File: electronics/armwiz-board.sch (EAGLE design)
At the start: 86 parts, among them J1 MICRO-SDCARD-CONNECTOR-330006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, U1 STM32F10XRXT6, U4 MIC5219-3.3V, X1 FH12-12S-1S, Y1 16MHz

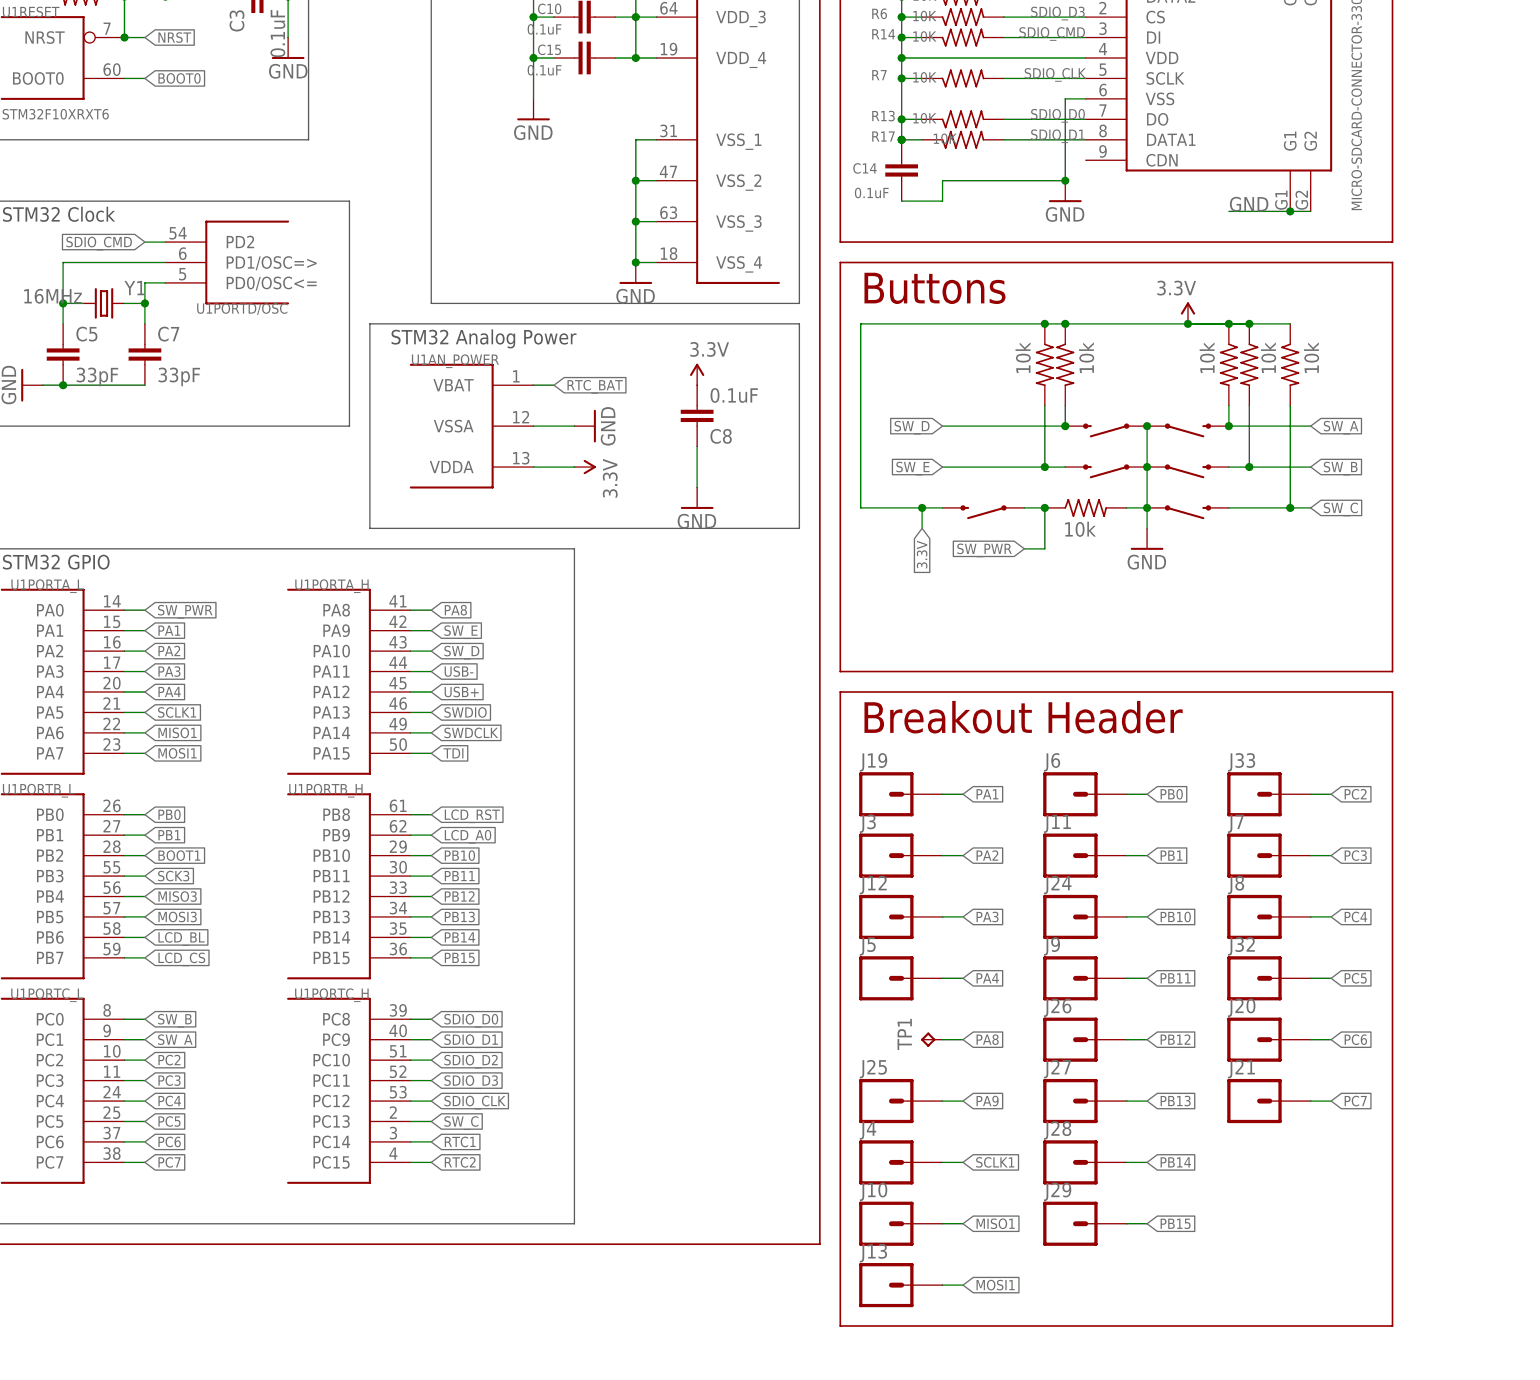
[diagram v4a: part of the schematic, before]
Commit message: reconfigured routing. Looks much better.
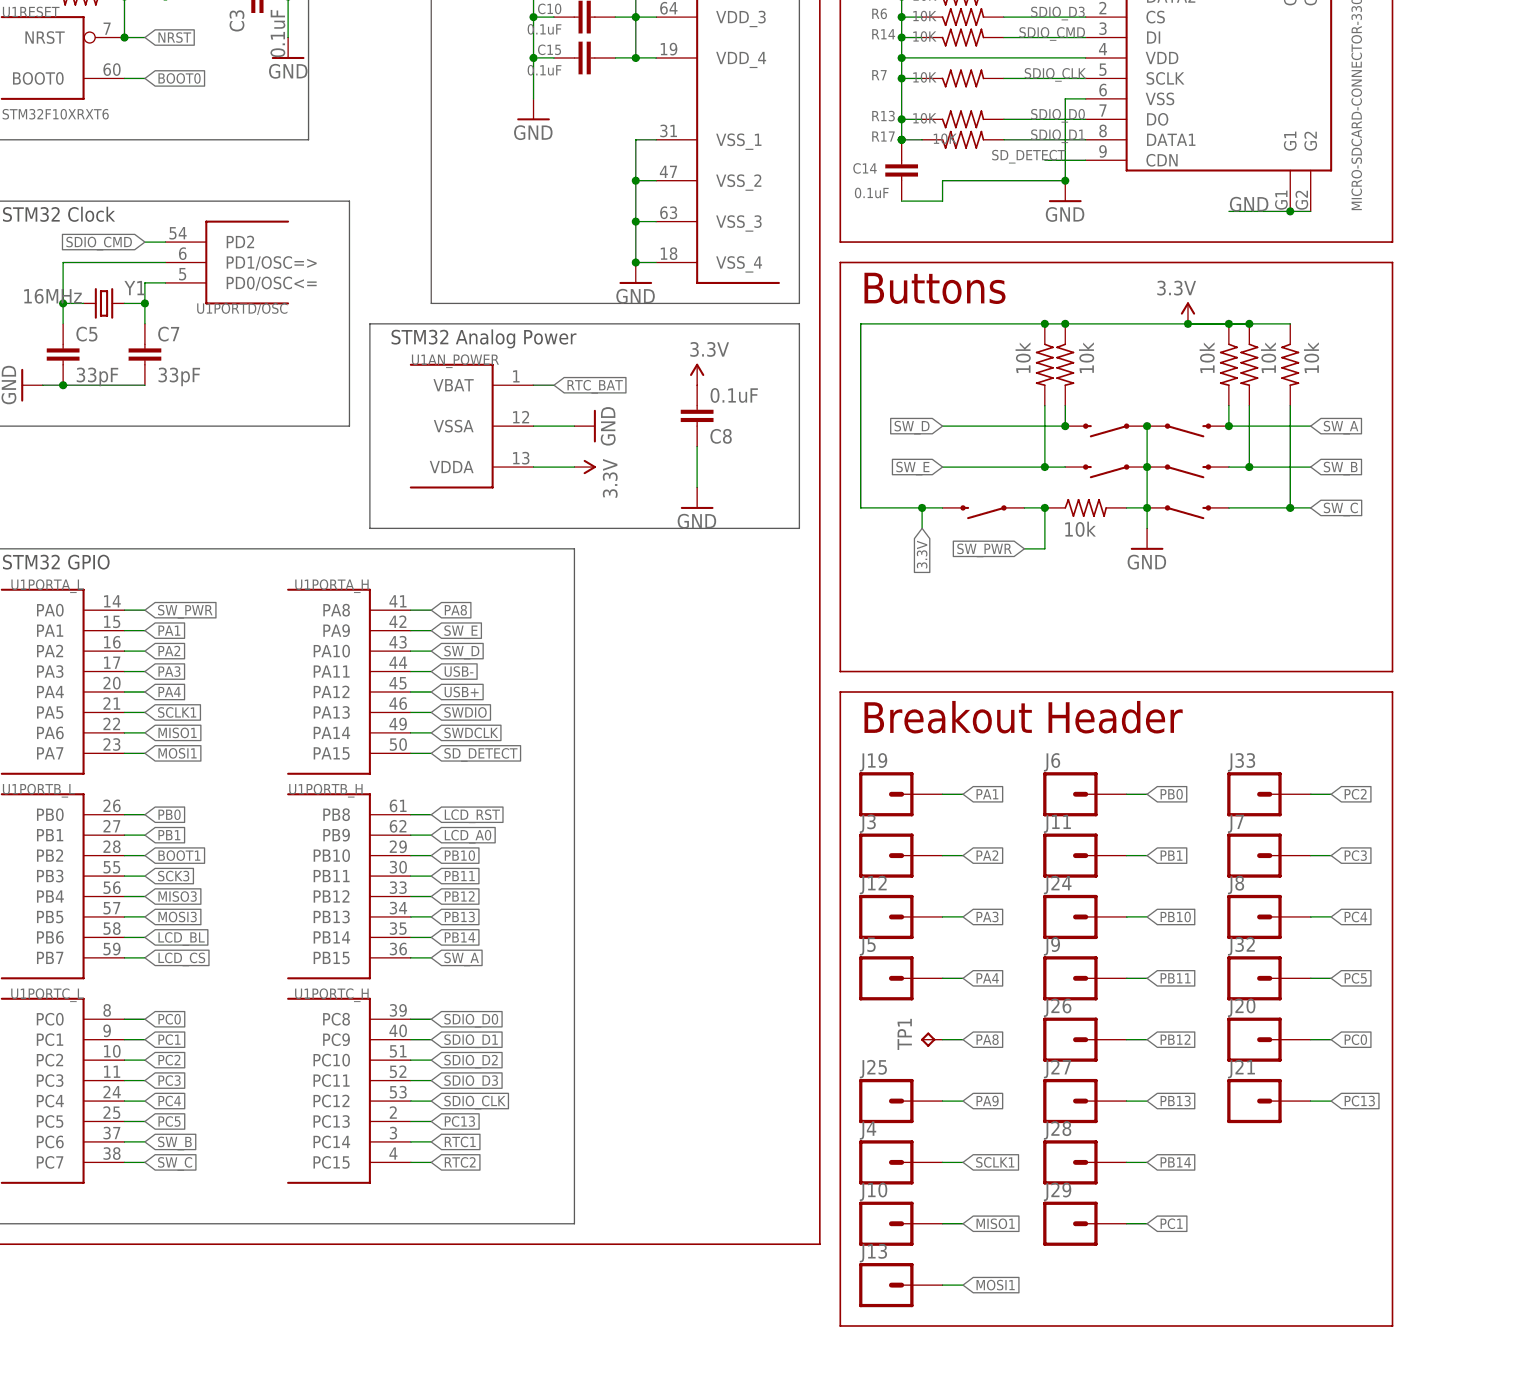
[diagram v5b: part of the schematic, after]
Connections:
- removed net PB15: J29.1, U1PORTB_H.PB15
- removed net PC6: J20.1, U1PORTC_L.PC6
- removed net PC7: J21.1, U1PORTC_L.PC7
- removed net TDI: U1PORTA_H.PA15
- new net PC0: J20.1, U1PORTC_L.PC0
- new net PC1: J29.1, U1PORTC_L.PC1
- new net PC13: J21.1, U1PORTC_H.PC13
- new net SD_DETECT: J1.CDN, U1PORTA_H.PA15
- net SW_A: now also U1PORTB_H.PB15; no longer U1PORTC_L.PC1
- net SW_B: now also U1PORTC_L.PC6; no longer U1PORTC_L.PC0
- net SW_C: now also U1PORTC_L.PC7; no longer U1PORTC_H.PC13
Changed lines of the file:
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@@
 </segment>
 <segment>
-<pinref part="U1" gate="PORTC_L" pin="PC0"/>
-<wire x1="27.94" y1="48.26" x2="30.48" y2="48.26" width="0.1524" layer="91"/>
-<label x="30.48" y="48.26" size="1.27" layer="95" xref="yes"/>
+<pinref part="U1" gate="PORTC_L" pin="PC6"/>
+<wire x1="27.94" y1="33.02" x2="30.48" y2="33.02" width="0.1524" layer="91"/>
+<label x="30.48" y="33.02" size="1.27" layer="95" xref="yes"/>
 </segment>
 </net>
@@
 </segment>
 <segment>
-<pinref part="U1" gate="PORTC_H" pin="PC13"/>
-<wire x1="63.5" y1="35.56" x2="66.04" y2="35.56" width="0.1524" layer="91"/>
-<label x="66.04" y="35.56" size="1.27" layer="95" xref="yes"/>
+<pinref part="U1" gate="PORTC_L" pin="PC7"/>
+<wire x1="27.94" y1="30.48" x2="30.48" y2="30.48" width="0.1524" layer="91"/>
+<label x="30.48" y="30.48" size="1.27" layer="95" xref="yes"/>
 </segment>
 </net>
@@
 </segment>
 <segment>
-<pinref part="U1" gate="PORTC_L" pin="PC1"/>
-<wire x1="27.94" y1="45.72" x2="30.48" y2="45.72" width="0.1524" layer="91"/>
-<label x="30.48" y="45.72" size="1.27" layer="95" xref="yes"/>
+<pinref part="U1" gate="PORTB_H" pin="PB15"/>
+<wire x1="63.5" y1="55.88" x2="66.04" y2="55.88" width="0.1524" layer="91"/>
+<label x="66.04" y="55.88" size="1.27" layer="95" xref="yes"/>
 </segment>
 </net>
@@
 </segment>
 </net>
-<net name="TDI" class="0">
-<segment>
-<pinref part="U1" gate="PORTA_H" pin="PA15"/>
-<wire x1="63.5" y1="81.28" x2="66.04" y2="81.28" width="0.1524" layer="91"/>
-<label x="66.04" y="81.28" size="1.27" layer="95" xref="yes"/>
-</segment>
-</net>
 <net name="SCLK1" class="0">
 <segment>
@@
 </segment>
 </net>
-<net name="PC6" class="0">
-<segment>
-<pinref part="U1" gate="PORTC_L" pin="PC6"/>
-<wire x1="27.94" y1="33.02" x2="30.48" y2="33.02" width="0.1524" layer="91"/>
-<label x="30.48" y="33.02" size="1.27" layer="95" xref="yes"/>
+<net name="PB14" class="0">
+<segment>
+<pinref part="U1" gate="PORTB_H" pin="PB14"/>
+<wire x1="63.5" y1="58.42" x2="66.04" y2="58.42" width="0.1524" layer="91"/>
+<label x="66.04" y="58.42" size="1.27" layer="95" xref="yes"/>
+</segment>
+<segment>
+<pinref part="J28" gate="G$1" pin="1"/>
+<wire x1="152.4" y1="30.48" x2="154.94" y2="30.48" width="0.1524" layer="91"/>
+<label x="154.94" y="30.48" size="1.27" layer="95" xref="yes"/>
+</segment>
+</net>
+<net name="PB13" class="0">
+<segment>
+<pinref part="U1" gate="PORTB_H" pin="PB13"/>
+<wire x1="63.5" y1="60.96" x2="66.04" y2="60.96" width="0.1524" layer="91"/>
+<label x="66.04" y="60.96" size="1.27" layer="95" xref="yes"/>
+</segment>
+<segment>
+<pinref part="J27" gate="G$1" pin="1"/>
+<wire x1="152.4" y1="38.1" x2="154.94" y2="38.1" width="0.1524" layer="91"/>
+<label x="154.94" y="38.1" size="1.27" layer="95" xref="yes"/>
+</segment>
+</net>
+<net name="PB12" class="0">
+<segment>
+<pinref part="U1" gate="PORTB_H" pin="PB12"/>
+<wire x1="63.5" y1="63.5" x2="66.04" y2="63.5" width="0.1524" layer="91"/>
+<label x="66.04" y="63.5" size="1.27" layer="95" xref="yes"/>
+</segment>
+<segment>
+<pinref part="J26" gate="G$1" pin="1"/>
+<wire x1="152.4" y1="45.72" x2="154.94" y2="45.72" width="0.1524" layer="91"/>
+<label x="154.94" y="45.72" size="1.27" layer="95" xref="yes"/>
+</segment>
+</net>
+<net name="PB11" class="0">
+<segment>
+<pinref part="U1" gate="PORTB_H" pin="PB11"/>
+<wire x1="63.5" y1="66.04" x2="66.04" y2="66.04" width="0.1524" layer="91"/>
+<label x="66.04" y="66.04" size="1.27" layer="95" xref="yes"/>
+</segment>
+<segment>
+<pinref part="J9" gate="G$1" pin="1"/>
+<wire x1="152.4" y1="53.34" x2="154.94" y2="53.34" width="0.1524" layer="91"/>
+<label x="154.94" y="53.34" size="1.27" layer="95" xref="yes"/>
+</segment>
+</net>
+<net name="PB10" class="0">
+<segment>
+<pinref part="U1" gate="PORTB_H" pin="PB10"/>
+<wire x1="63.5" y1="68.58" x2="66.04" y2="68.58" width="0.1524" layer="91"/>
+<label x="66.04" y="68.58" size="1.27" layer="95" xref="yes"/>
+</segment>
+<segment>
+<pinref part="J24" gate="G$1" pin="1"/>
+<wire x1="152.4" y1="60.96" x2="154.94" y2="60.96" width="0.1524" layer="91"/>
+<label x="154.94" y="60.96" size="1.27" layer="95" xref="yes"/>
+</segment>
+</net>
+<net name="PA9" class="0">
+<segment>
+<pinref part="J25" gate="G$1" pin="1"/>
+<wire x1="129.54" y1="38.1" x2="132.08" y2="38.1" width="0.1524" layer="91"/>
+<label x="132.08" y="38.1" size="1.27" layer="95" xref="yes"/>
+</segment>
+</net>
+<net name="PA8" class="0">
+<segment>
+<pinref part="U1" gate="PORTA_H" pin="PA8"/>
+<wire x1="63.5" y1="99.06" x2="66.04" y2="99.06" width="0.1524" layer="91"/>
+<label x="66.04" y="99.06" size="1.27" layer="95" xref="yes"/>
+</segment>
+<segment>
+<wire x1="129.54" y1="45.72" x2="132.08" y2="45.72" width="0.1524" layer="91"/>
+<label x="132.08" y="45.72" size="1.27" layer="95" xref="yes"/>
+<pinref part="TP1" gate="G$1" pin="TP"/>
+</segment>
+</net>
+<net name="SD_DETECT" class="0">
+<segment>
+<pinref part="J1" gate="J" pin="CDN"/>
+<wire x1="147.32" y1="154.94" x2="142.24" y2="154.94" width="0.1524" layer="91"/>
+<label x="144.78" y="154.94" size="1.27" layer="95" rot="MR0"/>
+</segment>
+<segment>
+<pinref part="U1" gate="PORTA_H" pin="PA15"/>
+<wire x1="63.5" y1="81.28" x2="66.04" y2="81.28" width="0.1524" layer="91"/>
+<label x="66.04" y="81.28" size="1.27" layer="95" xref="yes"/>
+</segment>
+</net>
+<net name="PC1" class="0">
+<segment>
+<pinref part="U1" gate="PORTC_L" pin="PC1"/>
+<wire x1="27.94" y1="45.72" x2="30.48" y2="45.72" width="0.1524" layer="91"/>
+<label x="30.48" y="45.72" size="1.27" layer="95" xref="yes"/>
+</segment>
+<segment>
+<pinref part="J29" gate="G$1" pin="1"/>
+<wire x1="152.4" y1="22.86" x2="154.94" y2="22.86" width="0.1524" layer="91"/>
+<label x="154.94" y="22.86" size="1.27" layer="95" xref="yes"/>
+</segment>
+</net>
+<net name="PC0" class="0">
+<segment>
+<pinref part="U1" gate="PORTC_L" pin="PC0"/>
+<wire x1="27.94" y1="48.26" x2="30.48" y2="48.26" width="0.1524" layer="91"/>
+<label x="30.48" y="48.26" size="1.27" layer="95" xref="yes"/>
 </segment>
 <segment>
@@
 </segment>
 </net>
-<net name="PC7" class="0">
-<segment>
-<pinref part="U1" gate="PORTC_L" pin="PC7"/>
-<wire x1="27.94" y1="30.48" x2="30.48" y2="30.48" width="0.1524" layer="91"/>
-<label x="30.48" y="30.48" size="1.27" layer="95" xref="yes"/>
+<net name="PC13" class="0">
+<segment>
+<pinref part="U1" gate="PORTC_H" pin="PC13"/>
+<wire x1="63.5" y1="35.56" x2="66.04" y2="35.56" width="0.1524" layer="91"/>
+<label x="66.04" y="35.56" size="1.27" layer="95" xref="yes"/>
 </segment>
 <segment>
@@
 </segment>
 </net>
-<net name="PB15" class="0">
-<segment>
-<pinref part="U1" gate="PORTB_H" pin="PB15"/>
-<wire x1="63.5" y1="55.88" x2="66.04" y2="55.88" width="0.1524" layer="91"/>
-<label x="66.04" y="55.88" size="1.27" layer="95" xref="yes"/>
-</segment>
-<segment>
-<pinref part="J29" gate="G$1" pin="1"/>
-<wire x1="152.4" y1="22.86" x2="154.94" y2="22.86" width="0.1524" layer="91"/>
-<label x="154.94" y="22.86" size="1.27" layer="95" xref="yes"/>
-</segment>
-</net>
-<net name="PB14" class="0">
-<segment>
-<pinref part="U1" gate="PORTB_H" pin="PB14"/>
-<wire x1="63.5" y1="58.42" x2="66.04" y2="58.42" width="0.1524" layer="91"/>
-<label x="66.04" y="58.42" size="1.27" layer="95" xref="yes"/>
-</segment>
-<segment>
-<pinref part="J28" gate="G$1" pin="1"/>
-<wire x1="152.4" y1="30.48" x2="154.94" y2="30.48" width="0.1524" layer="91"/>
-<label x="154.94" y="30.48" size="1.27" layer="95" xref="yes"/>
-</segment>
-</net>
-<net name="PB13" class="0">
-<segment>
-<pinref part="U1" gate="PORTB_H" pin="PB13"/>
-<wire x1="63.5" y1="60.96" x2="66.04" y2="60.96" width="0.1524" layer="91"/>
-<label x="66.04" y="60.96" size="1.27" layer="95" xref="yes"/>
-</segment>
-<segment>
-<pinref part="J27" gate="G$1" pin="1"/>
-<wire x1="152.4" y1="38.1" x2="154.94" y2="38.1" width="0.1524" layer="91"/>
-<label x="154.94" y="38.1" size="1.27" layer="95" xref="yes"/>
-</segment>
-</net>
-<net name="PB12" class="0">
-<segment>
-<pinref part="U1" gate="PORTB_H" pin="PB12"/>
-<wire x1="63.5" y1="63.5" x2="66.04" y2="63.5" width="0.1524" layer="91"/>
-<label x="66.04" y="63.5" size="1.27" layer="95" xref="yes"/>
-</segment>
-<segment>
-<pinref part="J26" gate="G$1" pin="1"/>
-<wire x1="152.4" y1="45.72" x2="154.94" y2="45.72" width="0.1524" layer="91"/>
-<label x="154.94" y="45.72" size="1.27" layer="95" xref="yes"/>
-</segment>
-</net>
-<net name="PB11" class="0">
-<segment>
-<pinref part="U1" gate="PORTB_H" pin="PB11"/>
-<wire x1="63.5" y1="66.04" x2="66.04" y2="66.04" width="0.1524" layer="91"/>
-<label x="66.04" y="66.04" size="1.27" layer="95" xref="yes"/>
-</segment>
-<segment>
-<pinref part="J9" gate="G$1" pin="1"/>
-<wire x1="152.4" y1="53.34" x2="154.94" y2="53.34" width="0.1524" layer="91"/>
-<label x="154.94" y="53.34" size="1.27" layer="95" xref="yes"/>
-</segment>
-</net>
-<net name="PB10" class="0">
-<segment>
-<pinref part="U1" gate="PORTB_H" pin="PB10"/>
-<wire x1="63.5" y1="68.58" x2="66.04" y2="68.58" width="0.1524" layer="91"/>
-<label x="66.04" y="68.58" size="1.27" layer="95" xref="yes"/>
-</segment>
-<segment>
-<pinref part="J24" gate="G$1" pin="1"/>
-<wire x1="152.4" y1="60.96" x2="154.94" y2="60.96" width="0.1524" layer="91"/>
-<label x="154.94" y="60.96" size="1.27" layer="95" xref="yes"/>
-</segment>
-</net>
-<net name="PA9" class="0">
-<segment>
-<pinref part="J25" gate="G$1" pin="1"/>
-<wire x1="129.54" y1="38.1" x2="132.08" y2="38.1" width="0.1524" layer="91"/>
-<label x="132.08" y="38.1" size="1.27" layer="95" xref="yes"/>
-</segment>
-</net>
-<net name="PA8" class="0">
-<segment>
-<pinref part="U1" gate="PORTA_H" pin="PA8"/>
-<wire x1="63.5" y1="99.06" x2="66.04" y2="99.06" width="0.1524" layer="91"/>
-<label x="66.04" y="99.06" size="1.27" layer="95" xref="yes"/>
-</segment>
-<segment>
-<wire x1="129.54" y1="45.72" x2="132.08" y2="45.72" width="0.1524" layer="91"/>
-<label x="132.08" y="45.72" size="1.27" layer="95" xref="yes"/>
-<pinref part="TP1" gate="G$1" pin="TP"/>
-</segment>
-</net>

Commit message: Plugging along.
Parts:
- removed C5, C7: 33pF, resistor:C-EUC0402K
- removed J25, J28, J29: (no value), SparkFun-Connectors:M01PTH
- removed S7: SWITCH-MOMENTARY-2-SMD-1101NE, PaxInstruments-Electromechanical:SWITCH-MOMENTARY-2-SMD-1101NE
- removed SJ1: (no value), SparkFun-Retired:SOLDERJUMPER_2WAYPASTE2&3
- removed TP1: TPB1,27, testpad:TPB1,27
- removed Y1: 16MHz, SparkFun-FreqCtrl:CRYSTALCRYSTAL-SMD-5X3-16MHZ
- removed Y2: (no value), SparkFun-FreqCtrl:CRYSTALCRYSTAL-SMD-5X3-16MHZ
- added J14: (no value), SparkFun-Connectors:M25PTH
- added LED2: GREEN, SparkFun-LED:LED0603
- added R18, R20: 100R, resistor:R-US_R0402
- added R21: 10K, resistor:R-US_R0402
- added R22: 360R, resistor:R-US_R0402
- added TP2, TP3, TP4: TPB1,27, testpad:TPB1,27
- added U$3: BL-5C-CONNECTOR, PaxInstruments-Connectors:BL-5C-CONNECTOR
- added U$7: ASDM1-16.000MHz-LCT, crystal:ASE
- added Y3: 32.768kHz, SparkFun-FreqCtrl:CRYSTAL3.2X1.5MM
- J2: value (none) -> CORTEX_DEBUGSMD; device SparkFun-Connectors:M04PTH -> SparkFun-Connectors:CORTEX_DEBUGSMD
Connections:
- removed net PA9: J25.1
- removed net PB12: J26.1, U1PORTB_H.PB12
- removed net PB13: J27.1, U1PORTB_H.PB13
- removed net PB14: J28.1, U1PORTB_H.PB14
- new net N$13: J2.SWDIO/TMS, R20.2
- new net N$17: J2.GNDDTCT
- new net OSC_IN: U$7.OUT, U1PORTD/OSC.PD0/OSC<=
- new net OSC_OUT: U$7.TRI, U1PORTD/OSC.PD1/OSC=>
- new net SWO: J2.SWO/TDO, U1PORTA_H.PA15
- new net USART1_RX: J26.1, TP3.TP, U1PORTA_H.PA10
- new net USART1_TX: J27.1, TP4.TP, U1PORTA_H.PA9
- net 3.3V: now also J2.VCC, U$7.VDD; no longer J2.4, SJ1.1
- net BOOT0: now also R21.2, TP2.TP; no longer SJ1.2
- net GND: now also J2.GND@3, J2.GND@5, J2.KEY, R21.1, R22.1, U$3.GND, U$3.P$4, U$3.P$5, U$7.GND; no longer C5.2, C7.2, J2.2, S7.1, SJ1.3
- net N$11: now also LED2.C, R22.2; no longer C7.1, U1PORTD/OSC.PD0/OSC<=, Y1.2
- net N$5: now also J2.SWDCLK/TCK, R18.2; no longer C5.1, U1PORTD/OSC.PD1/OSC=>, Y1.1
- net NRST: now also J2.NRESET; no longer S7.2
- net PA8: now also LED2.A; no longer TP1.TP
- net PC1: no longer J29.1
- net RTC1: now also Y3.2; no longer Y2.2
- net RTC2: now also Y3.1; no longer Y2.1
- net SD_DETECT: now also U1PORTB_H.PB14; no longer U1PORTA_H.PA15
- net SWDCLK: now also R18.1; no longer J2.3
- net SWDIO: now also R20.1; no longer J2.1
- net SW_D: now also U1PORTB_H.PB12; no longer U1PORTA_H.PA10
- net SW_E: now also U1PORTB_H.PB13; no longer U1PORTA_H.PA9
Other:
- note added: "BL-5C Battery"
- note added: "Boot config"
- note added: "Cortex Debug"
- note added: "TODO Add header for USART"
- note added: "TODO Add switch for BOOT0"
- note added: "TODO Make battery charging circuit"
- note removed: "Boot Config"
- moved on the sheet: BAT1, C1, C18, C2, C26, C27, C3, C35, C36, C4, C6, C9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
